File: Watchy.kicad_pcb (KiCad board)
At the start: 2 copper layers, 33.8 x 46 mm, 75 parts, among them J1 FPC24(0.5MM), J2 USB_C_Receptacle_USB2.0, J4 Conn_01x01, J5 Conn_01x01, M1 Vibration_Motor, Q1 AO3400A, Q2 UMH3N, Q4 CJ2301, Q5 S8050, SW1 BTN, SW2 BTN, SW3 BTN, SW4 BTN, U1 ESP32-PICO-D4, U2 ME6211C33M5G-N, U3 CP2102, U4 BMA423, U5 TP4054, U6 PCF8563BS, Y1 32.768KHz

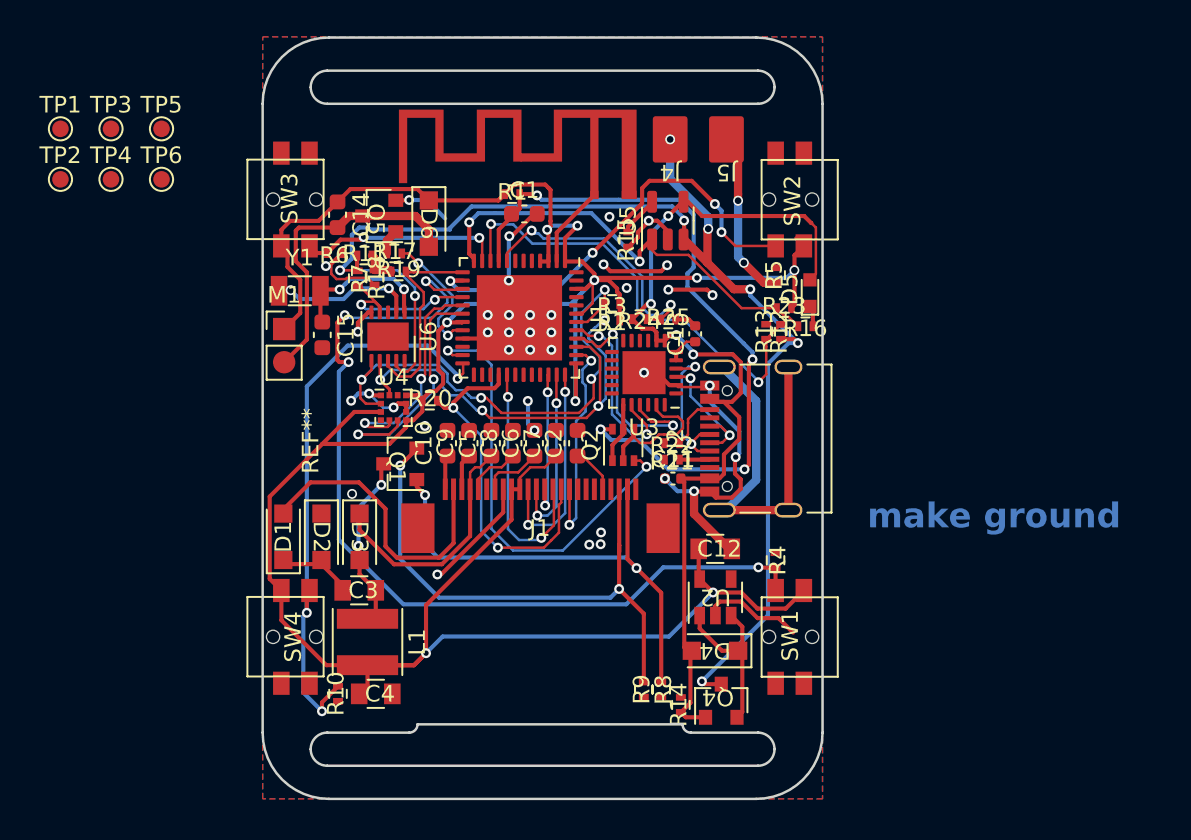
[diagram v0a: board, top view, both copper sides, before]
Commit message: Rerouting
Added testpoints
Made power traces wider
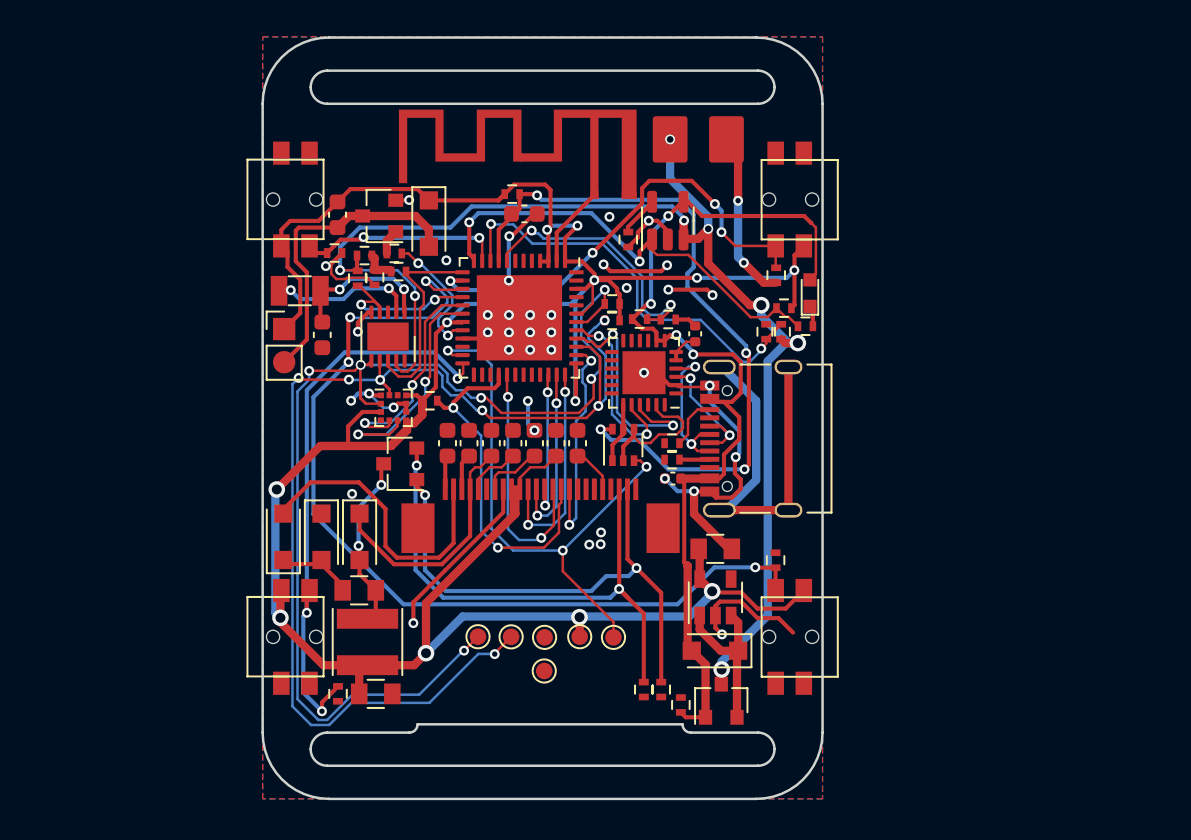
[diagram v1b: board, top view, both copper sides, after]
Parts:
- moved TP1 45.4 mm to (89.9, 106.4)
- moved TP4 39.5 mm to (87.8, 106.3)
- moved TP2 38.8 mm to (83.7, 106.3)
- moved TP5 38.4 mm to (85.7, 106.4)
- moved TP3 37.8 mm to (81.7, 106.3)
- moved TP6 37.6 mm to (85.7, 108.4)
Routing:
- net SCL: track 29.8 -> 70.7 mm, vias 4 -> 7
- net SDA: track 30.9 -> 69.2 mm, vias 4 -> 6
- net +3V3: track 173.3 -> 197.2 mm, vias 9 -> 12
- net GPIO0: track 26.8 -> 33.3 mm, vias 2 -> 3
- net ADC: track 27.6 -> 25.5 mm
- net GDR: track 30.0 -> 32.0 mm
- net GND: track 82.5 -> 84.1 mm, vias 41 -> 42
- net BTN_2: track 26.3 -> 27.7 mm
- net +BATT: track 81.9 -> 81.2 mm
- net RESE: track 34.2 -> 33.6 mm
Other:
- board text removed: "make ground"

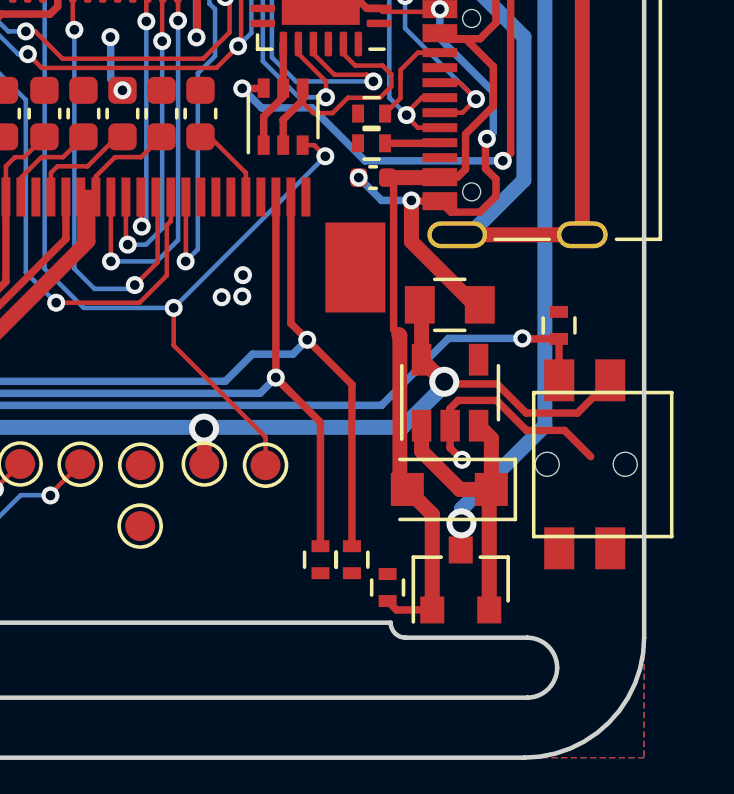
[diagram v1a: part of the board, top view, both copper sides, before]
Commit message: moved pull down resistors
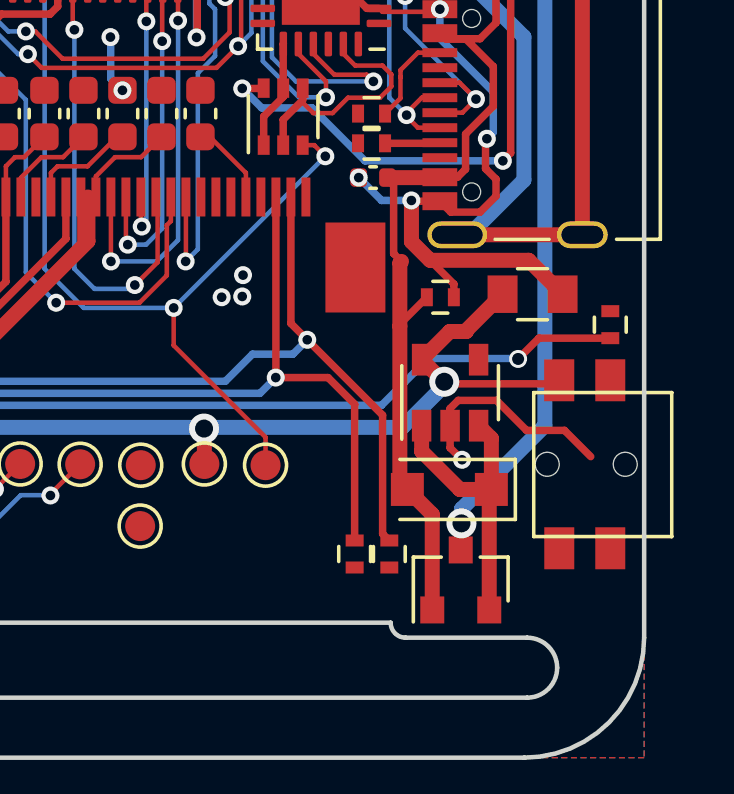
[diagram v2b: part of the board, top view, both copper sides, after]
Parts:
- moved R14 9.84 mm to (95.7, 100.8), turned to 0 degrees
- moved C12 2.78 mm to (98.8, 100.7)
- moved R4 1.71 mm to (101.4, 101.7)
- moved R8 1.26 mm to (94.0, 109.3)
- moved R9 1.16 mm to (92.8, 109.3)
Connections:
- SW1 pad 1: +3V3 -> BTN_1
- SW1 pad 2: BTN_1 -> +3V3
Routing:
- net GND: track 84.1 -> 88.2 mm
- net +3V3: track 197.2 -> 196.1 mm
- net RESE: track 33.6 -> 34.2 mm

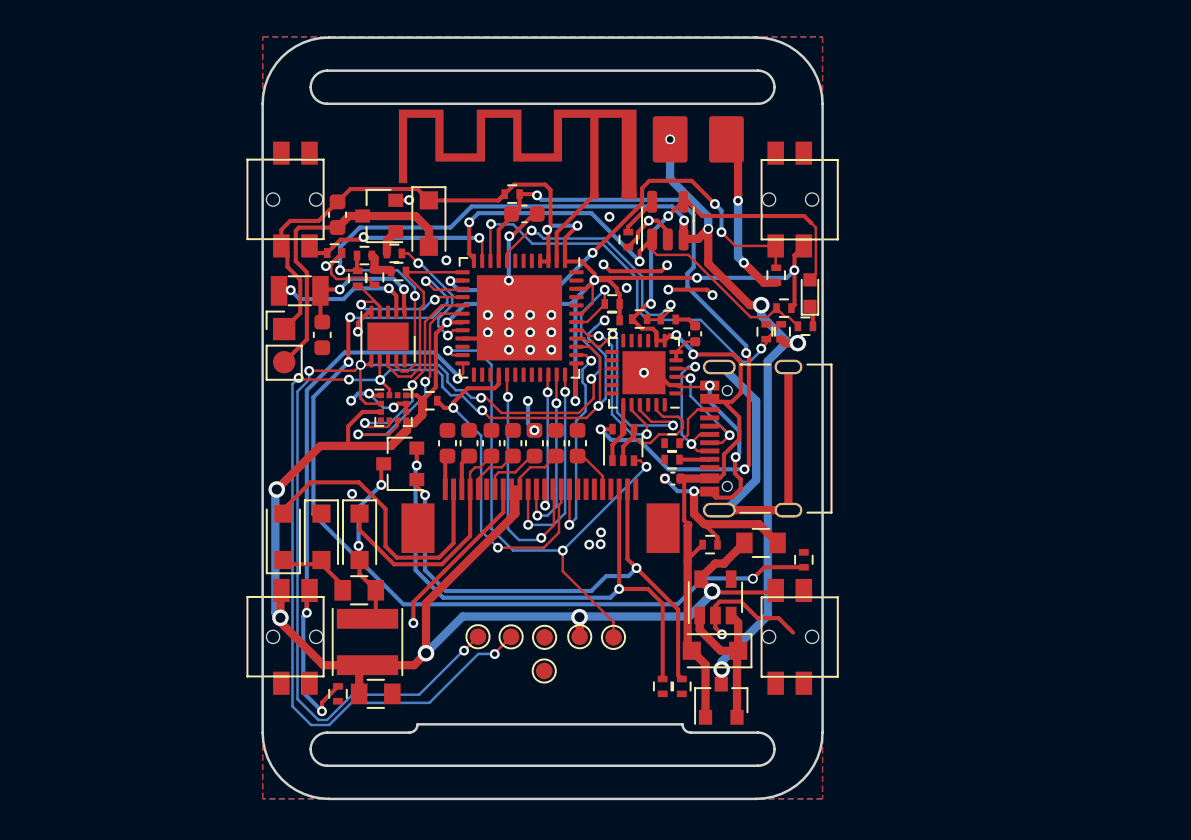
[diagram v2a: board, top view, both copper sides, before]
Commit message: Rev2.0
New Rev with ESP32-S3 and PCF2131
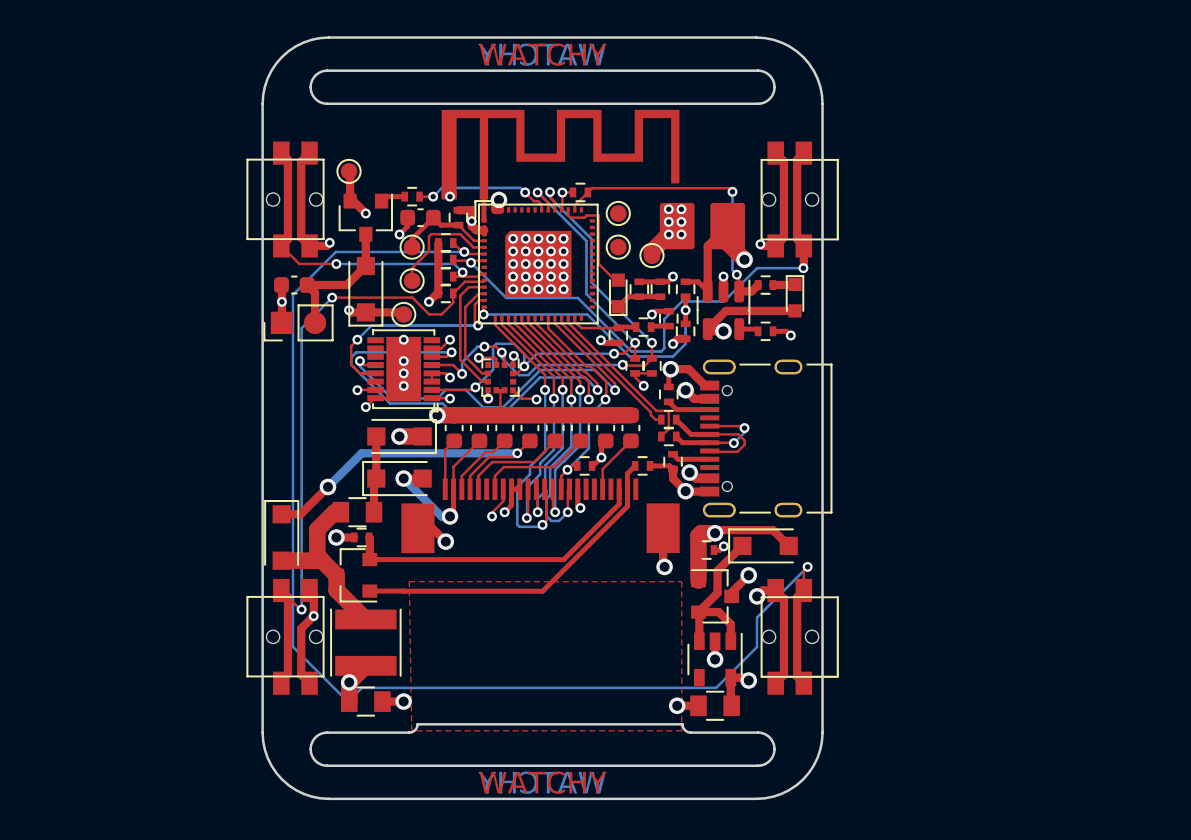
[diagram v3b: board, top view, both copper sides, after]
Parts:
- removed C14: 100nF, Capacitor_SMD:C_0603_1608Metric
- removed C15: 22pF, Capacitor_SMD:C_0603_1608Metric
- removed J5: Conn_01x01, Watchy:BatteryPads
- removed Q4: CJ2301, Watchy:SOT-23
- removed Q5: S8050, Watchy:SOT-23
- removed U6: PCF8563BS, Package_DFN_QFN:DFN-10-1EP_3x3mm_P0.5mm_EP1.7x2.5mm
- removed Y1: 32.768KHz, Crystal:Crystal_SMD_3215-2Pin_3.2x1.5mm
- added A1: ~, Watchy:logoLM, F.Cu at (88.9, 107.2)
- added D7: LED, Watchy:LED_0603, F.Cu at (90.2, 85.6)
- added J3: Conn_01x01, Watchy:BatteryPads, F.Cu at (96.8, 81.5)
- added Q3: CJ2301, Watchy:SOT-23, F.Cu at (96.0, 103.9)
- added R26: 1K, Watchy:R_0402, F.Cu at (92.7, 85.3)
- added REF**: OSHW-Logo2_7.3x6mm_SilkScreen, Symbol:OSHW-Logo2_7.3x6mm_SilkScreen, F.Cu at (81.8, 108.2)
- added TP7: GPIO0, TestPoint:TestPoint_Pad_D1.0mm, F.Cu at (77.7, 82.8)
- C11: value 4.7uF -> 1uF/50V; footprint Capacitor_SMD:C_0402_1005Metric -> Capacitor_SMD:C_0603_1608Metric
- C13: value 4.7uF -> 100nF; footprint Capacitor_SMD:C_0402_1005Metric -> Capacitor_SMD:C_0603_1608Metric
- Q2: value UMH3N -> S8050; footprint Package_TO_SOT_SMD:SOT-363_SC-70-6 -> Watchy:SOT-23
- R11: value 680K -> 4.7K
- R12, R19: value 100K -> 10K
- R14: value 10K -> 100K
- R17: value 1K -> 4.7K
- R18: value 220K -> 4.7K
- R2: value 4.7K -> 1K
- R23: value 10K -> 0
- R24: value 15k -> 0
- R25: value 22k -> 10K
- R3: value 4.7K -> 10K
- R5: value 10K -> 1K
- U1: value ESP32-PICO-D4 -> ~; footprint Package_DFN_QFN:QFN-48-1EP_7x7mm_P0.5mm_EP5.15x5.15mm -> Watchy:LGA56 (7x7mm)
- U2: value ME6211C33M5G-N -> TP4054; footprint Watchy:SOT-23-5 -> Package_TO_SOT_SMD:SOT-23-5
- U3: value CP2102 -> BMA423; footprint Package_DFN_QFN:QFN-24-1EP_4x4mm_P0.5mm_EP2.6x2.6mm -> Package_LGA:LGA-12_2x2mm_P0.5mm
- U4: value BMA423 -> ME6211C33M5G-N; footprint Package_LGA:LGA-12_2x2mm_P0.5mm -> Watchy:SOT-23-5
- U5: value TP4054 -> ~; footprint Package_TO_SOT_SMD:SOT-23-5 -> Watchy:HLSON16
- moved TP6 32.4 mm to (73.9, 78.2), turned to 90 degrees
- moved R4 28.9 mm to (79.8, 82.5), turned to 0 degrees
- moved TP2 26.4 mm to (90.2, 80.8), turned to 180 degrees
- moved R10 25.0 mm to (79.8, 85.6), turned to 0 degrees
- moved TP3 25.0 mm to (90.2, 82.8), turned to 180 degrees
- moved TP1 24.7 mm to (77.7, 84.8), turned to 90 degrees
- moved U4 24.7 mm to (96.0, 107.7), turned to -90 degrees
- moved C13 24.4 mm to (70.6, 85.1), turned to 0 degrees
- moved TP5 23.9 mm to (92.2, 83.3), turned to 90 degrees
- moved R5 22.5 mm to (77.7, 79.8), turned to 0 degrees
- moved TP4 22.2 mm to (77.2, 86.9), turned to 90 degrees
- moved Q2 20.7 mm to (74.9, 81.0), turned to -90 degrees
- moved R9 20.3 mm to (74.7, 100.3), turned to 0 degrees
- moved U5 18.3 mm to (77.2, 90.2), turned to 180 degrees
- moved R11 17.6 mm to (91.2, 90.0), turned to 90 degrees
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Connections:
- C11 pad 1: GND -> PREVGL
- C11 pad 2: VBUS -> GND
- C13 pad 1: Net-(U3-VDD) -> +3V3
- C13 pad 2: GND -> Net-(D6-A)
- C3 pad 1: Net-(D1-K) -> Net-(D3-A)
- C3 pad 2: Net-(D3-A) -> Net-(D1-K)
- J2 pad A6: Net-(U3-D+) -> Net-(J2-D+-PadA6)
- J2 pad A7: Net-(U3-D-) -> Net-(J2-D--PadA7)
- J2 pad B6: Net-(U3-D+) -> Net-(J2-D+-PadA6)
- J2 pad B7: Net-(U3-D-) -> Net-(J2-D--PadA7)
- J4 pad 1: +BATT -> GND
- L1 pad 1: Net-(D3-A) -> +3V3
- L1 pad 2: +3V3 -> Net-(D3-A)
- Q2 pad 1: RTS -> Net-(Q2-B)
- Q2 pad 2: DTR -> GND
- Q2 pad 3: GPIO0 -> Net-(D6-A)
- R11 pad 1: +BATT -> +3V3
- R11 pad 2: Net-(R11-Pad2) -> SCL
- R12 pad 1: +BATT -> VBUS
- R12 pad 2: ADC -> GND
- R13 pad 1: ADC -> +BATT
- R13 pad 2: GND -> BAT_ADC
- R14 pad 1: VBUS -> BAT_ADC
- R15 pad 2: Net-(U5-PROG) -> Net-(U2-PROG)
- R16 pad 1: Net-(D5-K) -> BATT_STAT
- R16 pad 2: BATT_STAT -> Net-(D5-K)
- R17 pad 1: Net-(Q5-B) -> +3V3
- R17 pad 2: VIB_PWM -> SDA
- R18 pad 1: Net-(R11-Pad2) -> Net-(U1-GPIO21)
- R18 pad 2: GND -> Net-(R18-Pad2)
- R19 pad 1: Net-(R11-Pad2) -> Net-(U1-GPIO21)
- R19 pad 2: 32KHZ -> VBUS
- R2 pad 1: +3V3 -> GND
- R2 pad 2: SCL -> Net-(D7-K)
- R23 pad 1: BATT_STAT -> Net-(J2-D--PadA7)
- R23 pad 2: +3V3 -> D-
- R24 pad 1: Net-(U1-SENSOR_VN) -> Net-(J2-D+-PadA6)
- R24 pad 2: VBUS -> D+
- R25 pad 1: Net-(U1-SENSOR_VN) -> GND
- R25 pad 2: GND -> Net-(R18-Pad2)
- R3 pad 1: +3V3 -> BATT_STAT
- R3 pad 2: SDA -> +3V3
- R5 pad 1: GND -> Net-(Q2-B)
- R5 pad 2: BTN_2 -> VIB_PWM
- R6 pad 2: BTN_3 -> BTN_2
- R7 pad 1: +BATT -> GND
- R7 pad 2: RTC_INT -> BTN_3
- SW2 pad 1: +3V3 -> BTN_2
- SW2 pad 2: BTN_2 -> +3V3
- SW3 pad 1: +3V3 -> BTN_3
- SW3 pad 2: BTN_3 -> +3V3
- SW4 pad 1: +3V3 -> BTN_4
- SW4 pad 2: BTN_4 -> +3V3
- U1 pad 1: +3V3 -> Net-(AE1-FEED)
- U1 pad 10: ADC -> BTN_4
- U1 pad 11: BTN_3 -> ACC_INT_2
- U1 pad 12: BATT_STAT -> ACC_INT_1
- U1 pad 13: 32KHZ -> RTC_INTA
- U1 pad 14: BTN_2 -> BAT_ADC
- U1 pad 15: BTN_1 -> SS
- U1 pad 16: RTC_INT -> MOSI
- U1 pad 17: ACC_INT_1 -> SCK
- U1 pad 18: ACC_INT_2 -> BUSY
- U1 pad 19: +3V3 -> DC
- U1 pad 2: Net-(AE1-FEED) -> +3V3
- U1 pad 20: VIB_PWM -> +3V3
- U1 pad 21: GND -> CLK_32kHz
- U1 pad 23: GPIO0 -> RES
- U1 pad 24: BTN_4 -> RTC_INTB
- U1 pad 25: unconnected-(U1-IO16-Pad25) -> D-
- U1 pad 26: unconnected-(U1-VDD_SDIO-Pad26) -> D+
- U1 pad 27: unconnected-(U1-IO17-Pad27) -> Net-(U1-GPIO21)
- U1 pad 28: RES -> unconnected-(U1-SPICS1-Pad28)
- U1 pad 29: DC -> unconnected-(U1-VDD_SPI-Pad29)
- U1 pad 30: unconnected-(U1-CMD-Pad30) -> (no net)
- U1 pad 31: unconnected-(U1-CLK-Pad31) -> (no net)
- U1 pad 32: unconnected-(U1-SD0-Pad32) -> (no net)
- U1 pad 33: unconnected-(U1-SD1-Pad33) -> (no net)
- U1 pad 34: SS -> (no net)
- U1 pad 35: SCK -> (no net)
- U1 pad 36: MOSI -> unconnected-(U1-SPICLK_N-Pad36)
- U1 pad 37: +3V3 -> unconnected-(U1-SPICLK_P-Pad37)
- U1 pad 38: BUSY -> unconnected-(U1-GPIO33-Pad38)
- U1 pad 39: SCL -> unconnected-(U1-GPIO34-Pad39)
- U1 pad 4: +3V3 -> EN
- U1 pad 40: RX -> unconnected-(U1-GPIO35-Pad40)
- U1 pad 41: TX -> unconnected-(U1-GPIO36-Pad41)
- U1 pad 42: SDA -> unconnected-(U1-GPIO37-Pad42)
- U1 pad 43: +3V3 -> unconnected-(U1-GPIO38-Pad43)
- U1 pad 44: unconnected-(U1-XTAL_N_NC-Pad44) -> BATT_STAT
- U1 pad 45: unconnected-(U1-XTAL_P_NC-Pad45) -> LED
- U1 pad 47: unconnected-(U1-CAP2_NC-Pad47) -> SDA
- U1 pad 48: unconnected-(U1-CAP1_NC-Pad48) -> SCL
- U1 pad 49: GND -> VIB_PWM
- U1 pad 5: unconnected-(U1-SENSOR_VP-Pad5) -> GPIO0
- U1 pad 6: unconnected-(U1-SENSOR_CAPP-Pad6) -> BTN_1
- U1 pad 7: unconnected-(U1-SENSOR_CAPN-Pad7) -> BTN_2
- U1 pad 8: Net-(U1-SENSOR_VN) -> unconnected-(U1-GPIO3-Pad8)
- U1 pad 9: EN -> BTN_3
- U2 pad 1: Net-(D4-K) -> BATT_STAT
- U2 pad 3: Net-(D4-K) -> +BATT
- U2 pad 4: unconnected-(U2-NC-Pad4) -> VBUS
- U2 pad 5: +3V3 -> Net-(U2-PROG)
- U3 pad 1: unconnected-(U3-RI-Pad1) -> GND
- U3 pad 10: unconnected-(U3-VIO/NC-Pad10) -> +3V3
- U3 pad 12: unconnected-(U3-GPIO.2-Pad12) -> SCL
- U3 pad 2: GND -> SDA
- U3 pad 3: Net-(U3-D+) -> +3V3
- U3 pad 4: Net-(U3-D-) -> unconnected-(U3-ASDA-Pad4)
- U3 pad 5: Net-(U3-VDD) -> ACC_INT_1
- U3 pad 6: Net-(U3-VDD) -> ACC_INT_2
- U3 pad 7: VBUS -> +3V3
- U3 pad 8: VBUS -> GND
- U3 pad 9: unconnected-(U3-~{RST}-Pad9) -> GND
- U4 pad 1: GND -> Net-(D4-K)
- U4 pad 2: SDA -> GND
- U4 pad 3: +3V3 -> Net-(D4-K)
- U4 pad 5: ACC_INT_1 -> +3V3
- U5 pad 1: BATT_STAT -> +3V3
- U5 pad 2: GND -> SCL
- U5 pad 3: +BATT -> GND
- U5 pad 4: VBUS -> GND
- U5 pad 5: Net-(U5-PROG) -> SDA
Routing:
- net +3V3: track 196.1 -> 63.1 mm, vias 12 -> 20
- net +BATT: track 81.2 -> 30.1 mm, vias 8 -> 2
- net SCL: track 70.7 -> 30.5 mm, vias 7 -> 5
- net SDA: track 69.2 -> 30.6 mm
- net EN: track 43.2 -> 5.96 mm, vias 4 -> 0
- net CLK_32kHz: track 0.00 -> 31.1 mm, vias 0 -> 2
- net GND: track 88.2 -> 58.9 mm, vias 42 -> 61
- net GPIO0: track 33.3 -> 6.82 mm, vias 3 -> 0
- net RTC_INTB: track 0.00 -> 25.5 mm, vias 0 -> 2
- net ADC: track 25.5 -> 0.00 mm, vias 2 -> 0
- net BTN_1: track 56.5 -> 78.8 mm, vias 4 -> 2
- net RTC_INTA: track 0.00 -> 19.8 mm, vias 0 -> 2
- net BAT_ADC: track 0.00 -> 17.7 mm, vias 0 -> 2
- net Net-(U1-SENSOR_VN): track 16.4 -> 0.00 mm, vias 2 -> 0
- net RESE: track 34.2 -> 18.7 mm, vias 2 -> 0
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- added copper zone on F.Cu, net (none)
- added copper zone on In2.Cu, net +3V3
- added copper zone on In1.Cu, net GND
- removed copper zone on B.Cu, net GND
- removed copper zone on F.Cu, net GND
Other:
- copper layers 2 -> 4
- board text added: "WatchyLT Rev 2.0 01/24"
- board text added: "https://github.com/ etwasmitbaum/ watchy-hardware"

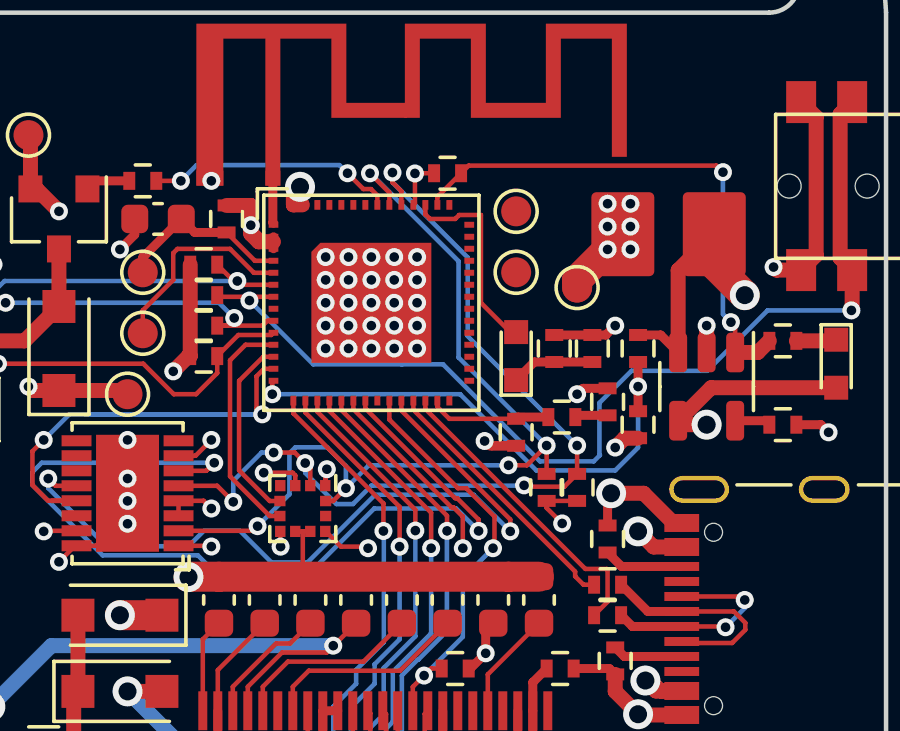
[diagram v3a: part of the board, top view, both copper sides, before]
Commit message: Cleanup and connection of I2C test points
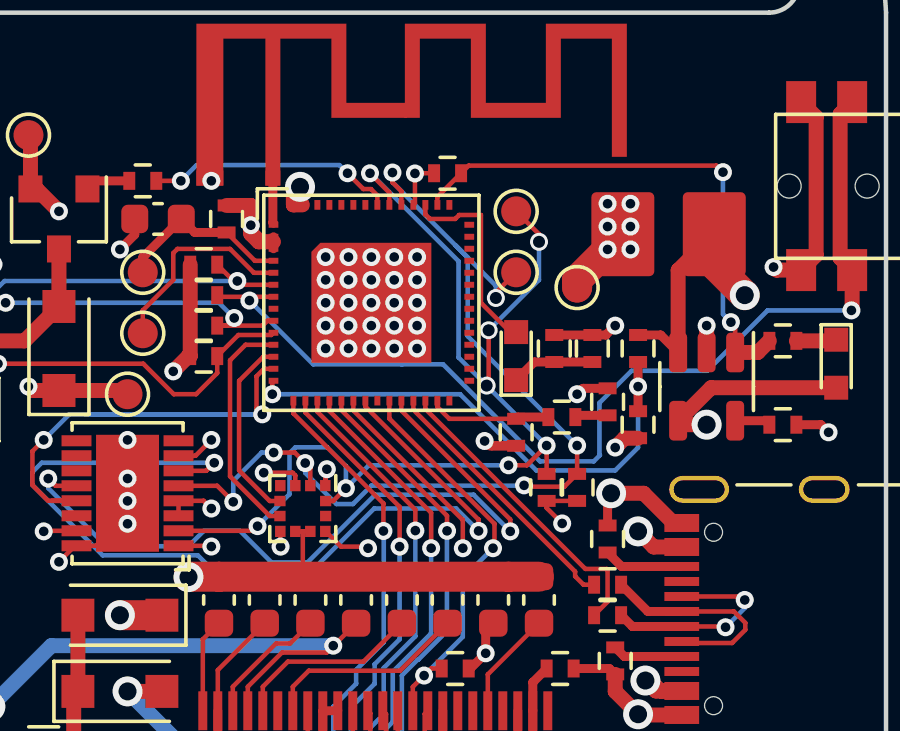
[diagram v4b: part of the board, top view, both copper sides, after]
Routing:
- net SCL: track 30.5 -> 37.3 mm, vias 5 -> 8
- net SDA: track 30.6 -> 34.0 mm, vias 6 -> 7
